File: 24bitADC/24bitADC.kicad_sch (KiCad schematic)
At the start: 12 parts, among them J1 USB_A, J2 Conn_01x04_Socket, Q1 MMBT3906, U1 HX711

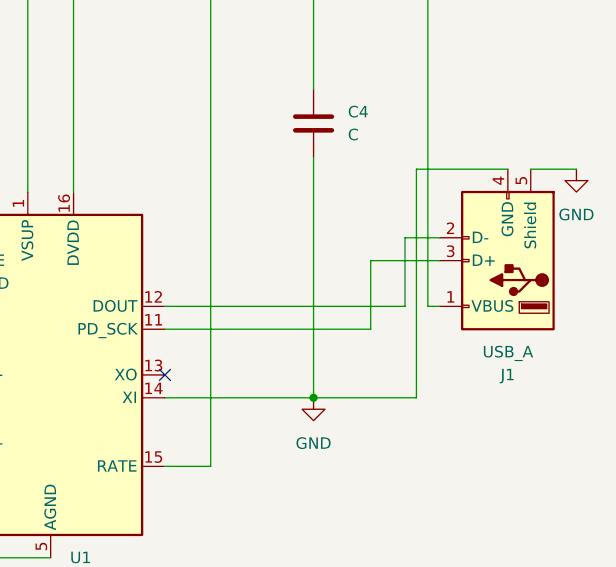
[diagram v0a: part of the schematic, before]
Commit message: Switch D- D+
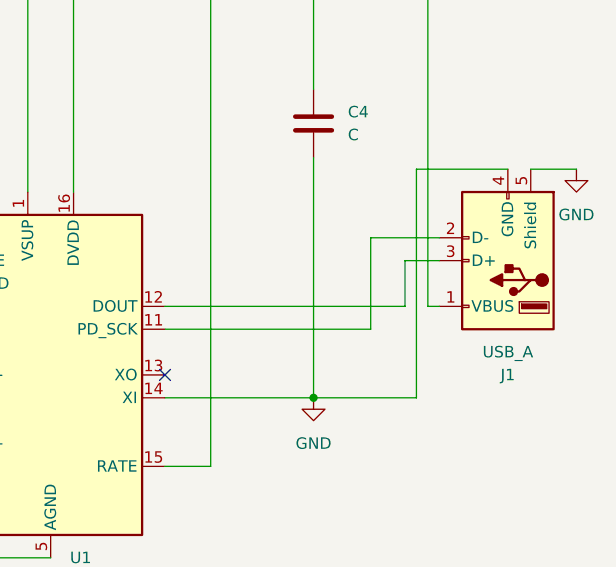
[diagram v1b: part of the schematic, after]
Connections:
- net at J1.2 (D-): now also U1.11 (PD_SCK); no longer U1.12 (DOUT)
- net at J1.3 (D+): now also U1.12 (DOUT); no longer U1.11 (PD_SCK)
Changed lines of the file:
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@@
-	(wire
-		(pts
-			(xy 186.69 92.71) (xy 194.31 92.71)
-		)
-		(stroke
-			(width 0)
-			(type default)
-		)
-	)
 	(wire
 		(pts
@@
 	(wire
 		(pts
+			(xy 190.5 92.71) (xy 194.31 92.71)
+		)
+		(stroke
+			(width 0)
+			(type default)
+		)
+	)
+	(wire
+		(pts
 			(xy 163.83 107.95) (xy 180.34 107.95)
 		)
@@
 	(wire
 		(pts
-			(xy 186.69 100.33) (xy 186.69 92.71)
+			(xy 186.69 90.17) (xy 186.69 100.33)
 		)
 		(stroke
@@
 	(wire
 		(pts
-			(xy 190.5 90.17) (xy 194.31 90.17)
-		)
-		(stroke
-			(width 0)
-			(type default)
-		)
-	)
-	(wire
-		(pts
 			(xy 151.13 125.73) (xy 130.81 125.73)
 		)
@@
 	(wire
 		(pts
+			(xy 186.69 90.17) (xy 194.31 90.17)
+		)
+		(stroke
+			(width 0)
+			(type default)
+		)
+	)
+	(wire
+		(pts
 			(xy 163.83 97.79) (xy 190.5 97.79)
 		)
@@
 	(wire
 		(pts
+			(xy 190.5 97.79) (xy 190.5 92.71)
+		)
+		(stroke
+			(width 0)
+			(type default)
+		)
+	)
+	(wire
+		(pts
 			(xy 138.43 105.41) (xy 138.43 100.33)
 		)
 		(stroke
-			(width 0)
-			(type default)
-		)
-	)
-	(wire
-		(pts
-			(xy 190.5 97.79) (xy 190.5 90.17)
-		)
-		(stroke

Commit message: 基盤作成
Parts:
- C1, C2: footprint (none) -> Capacitor_SMD:C_0201_0603Metric_Pad0.64x0.40mm_HandSolder
- C3, C4: footprint (none) -> Capacitor_SMD:C_0402_1005Metric_Pad0.74x0.62mm_HandSolder
- J1: footprint (none) -> TORICA_Hardwarelib:USB_A_4P_Female
- J2: footprint (none) -> CN2_CN3:24bitADC_CN2_CN3
- R1, R2, R3, R4: footprint (none) -> Resistor_SMD:R_0603_1608Metric_Pad0.98x0.95mm_HandSolder
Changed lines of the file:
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@@
 			)
 		)
-		(property "Footprint" ""
+		(property "Footprint" "Capacitor_SMD:C_0201_0603Metric_Pad0.64x0.40mm_HandSolder"
 			(at 138.43 119.6848 0)
 			(effects
@@
 			)
 		)
-		(property "Footprint" ""
+		(property "Footprint" "TORICA_Hardwarelib:USB_A_4P_Female"
 			(at 198.12 91.44 0)
 			(effects
@@
 			)
 		)
-		(property "Footprint" ""
+		(property "Footprint" "Resistor_SMD:R_0603_1608Metric_Pad0.98x0.95mm_HandSolder"
 			(at 108.712 76.2 90)
 			(effects
@@
 			)
 		)
-		(property "Footprint" ""
+		(property "Footprint" "CN2_CN3:24bitADC_CN2_CN3"
 			(at 54.61 57.15 0)
 			(effects
@@
 			)
 		)
-		(property "Footprint" ""
+		(property "Footprint" "Capacitor_SMD:C_0402_1005Metric_Pad0.74x0.62mm_HandSolder"
 			(at 102.5652 86.36 0)
 			(effects
@@
 			)
 		)
-		(property "Footprint" ""
+		(property "Footprint" "Resistor_SMD:R_0603_1608Metric_Pad0.98x0.95mm_HandSolder"
 			(at 127 102.108 90)
 			(effects
@@
 			)
 		)
-		(property "Footprint" ""
+		(property "Footprint" "Resistor_SMD:R_0603_1608Metric_Pad0.98x0.95mm_HandSolder"
 			(at 127 109.728 90)
 			(effects
@@
 			)
 		)
-		(property "Footprint" ""
+		(property "Footprint" "Resistor_SMD:R_0603_1608Metric_Pad0.98x0.95mm_HandSolder"
 			(at 108.712 88.9 90)
 			(effects
@@
 			)
 		)
-		(property "Footprint" ""
+		(property "Footprint" "Capacitor_SMD:C_0402_1005Metric_Pad0.74x0.62mm_HandSolder"
 			(at 181.3052 81.28 0)
 			(effects
@@
 			)
 		)
-		(property "Footprint" ""
+		(property "Footprint" "Capacitor_SMD:C_0201_0603Metric_Pad0.64x0.40mm_HandSolder"
 			(at 135.5852 107.95 0)
 			(effects
